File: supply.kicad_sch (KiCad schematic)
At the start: 43 parts, among them Q21 BC817-25W, Q22 BC817-25W, Q23 BSS84AKW, Q5 BC817-25W, U30 AP62301_TSOT, U4 TLV70012_SC70, U5 TLV70018_SC70, U6 TLV70025_SC70

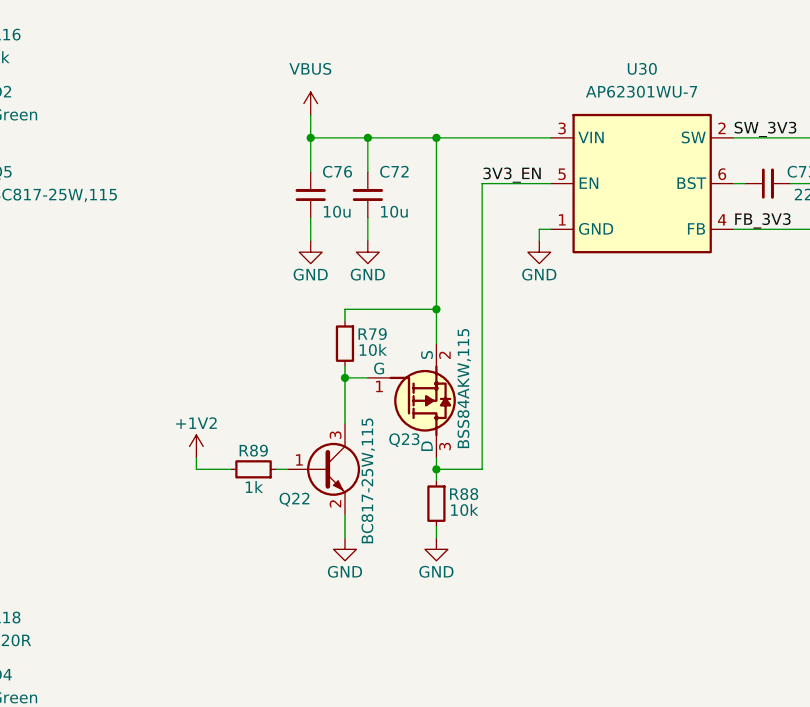
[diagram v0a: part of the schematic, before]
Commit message: [#72133] Update USB FTDI sheet
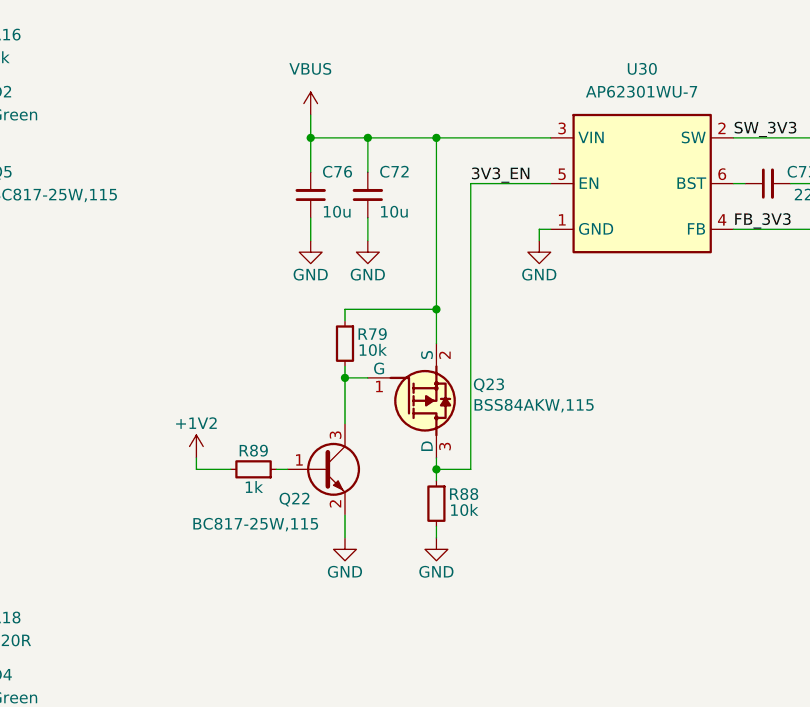
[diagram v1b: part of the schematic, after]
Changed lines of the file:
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@@
 	(wire
 		(pts
-			(xy 185.42 134.62) (xy 185.42 102.87)
+			(xy 184.15 134.62) (xy 184.15 102.87)
 		)
 		(stroke
@@
 	(wire
 		(pts
-			(xy 180.34 134.62) (xy 185.42 134.62)
+			(xy 180.34 134.62) (xy 184.15 134.62)
 		)
 		(stroke
@@
 	(wire
 		(pts
-			(xy 185.42 102.87) (xy 193.04 102.87)
+			(xy 184.15 102.87) (xy 193.04 102.87)
 		)
 		(stroke
@@
 	)
 	(label "3V3_EN"
-		(at 185.42 102.87 0)
+		(at 184.15 102.87 0)
 		(fields_autoplaced yes)
 		(effects
@@
 		(dnp no)
 		(property "Reference" "Q23"
-			(at 175.006 131.318 0)
+			(at 184.404 125.222 0)
 			(effects
 				(font
@@
 		)
 		(property "MPN" "BSS84AKW,115"
-			(at 183.388 118.872 90)
+			(at 184.404 127.508 0)
 			(effects
 				(font
@@
 		)
 		(property "MPN" "BC817-25W,115"
-			(at 172.72 143.002 90)
+			(at 153.162 140.716 0)
 			(effects
 				(font

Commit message: [#72447] SCH: Update matrix drive resistors
Signed-off-by: Dawid Lentka <dlentka@antmicro.com>
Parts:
- R18: value R_120R_0402 -> R_120R_0603; footprint antmicro-footprints:R_0402_1005Metric -> antmicro-footprints:R_0603_1608Metric; symbol antmicroResistors0402:R_120R_0402 -> antmicroResistors0603:R_120R_0603; MPN CR0402-FX-1200GLF -> CR0603-FX-1200ELF
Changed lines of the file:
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@@
 	(title_block
 		(title "LED Panel Board")
-		(date "2025-01-31")
+		(date "2025-02-04")
 		(rev "1.0.0")
 	)
@@
 	)
 	(symbol
-		(lib_id "antmicroResistors0402:R_120R_0402")
+		(lib_id "antmicroResistors0603:R_120R_0603")
 		(at 128.27 154.94 270)
 		(mirror x)
@@
 			)
 		)
-		(property "Value" "R_120R_0402"
+		(property "Value" "R_120R_0603"
 			(at 115.57 134.62 0)
 			(effects
@@
 			)
 		)
-		(property "Footprint" "antmicro-footprints:R_0402_1005Metric"
+		(property "Footprint" "antmicro-footprints:R_0603_1608Metric"
 			(at 113.03 134.62 0)
 			(effects
@@
 			)
 		)
-		(property "Description" "SMD Chip Resistor, 120 ohm, ± 1%, 63 mW, 0402 [1005 Metric], Thick Film, General Purpose"
+		(property "Description" "SMD Chip Resistor, 120 ohm, ± 1%, 100 mW, 0603 [1608 Metric], Thick Film, General Purpose"
 			(at 128.27 154.94 0)
 			(effects
@@
 			)
 		)
-		(property "MPN" "CR0402-FX-1200GLF"
+		(property "MPN" "CR0603-FX-1200ELF"
 			(at 107.95 134.62 0)
 			(effects
